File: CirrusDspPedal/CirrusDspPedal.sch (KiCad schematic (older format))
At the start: 0 parts

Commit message: Completed schematic design
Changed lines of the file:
@@
 $Descr A4 11693 8268
 encoding utf-8
-Sheet 1 10
+Sheet 1 11
 Title ""
 Date ""
@@
 F0 "SignalRelay" 50
 F1 "SignalRelay.sch" 50
-F2 "SignalSwitch" I L 5075 1750 50
-F3 "SIGNAL_IN" I L 5075 1300 50
-F4 "SIGNAL_OUT" I R 7050 1300 50
-F5 "FX_IN" I L 5075 1525 50
-F6 "FX_OUT" I R 7050 1525 50
+F2 "SIGNAL_IN" I L 5075 1300 50
+F3 "SIGNAL_OUT" I R 7050 1300 50
+F4 "FX_IN" I L 5075 1525 50
+F5 "FX_OUT" I R 7050 1525 50
+F6 "RelayCoil_OUT" I L 5075 1750 50
 $EndSheet
 Wire Wire Line
@@
 F8 "I2S_LRCK_OUT" I R 7050 3175 50
 F9 "I2S_LRCK_IN" I L 5050 3175 50
-F10 "ExpInput" I L 5050 4325 50
-F11 "SIgnalSwitch" I L 5050 2550 50
-F12 "FootSwitchA" I L 5050 4500 50
-F13 "FootSwitchB" I L 5050 4675 50
-F14 "UserPotA" I L 5050 4850 50
-F15 "UserPotB" I L 5050 5025 50
-F16 "UserSwA" I L 5050 5200 50
-F17 "UserSwB" I L 5050 5375 50
+F10 "UserSwitchB_IN" I L 5050 5375 50
+F11 "UserSwithA_IN" I L 5050 5200 50
+F12 "RelayCoil_OUT" I L 5050 2550 50
+F13 "FootExp_IN" I L 5050 4325 50
+F14 "UserPotA_IN" I L 5050 4850 50
+F15 "UserPotB_IN" I L 5050 5025 50
+F16 "FootSwitchB_IN" I L 5050 4675 50
+F17 "FootSwitchA_IN" I L 5050 4500 50
+F18 "uSD_CMD" I R 7050 4725 50
+F19 "uSD_CLK" I R 7050 4850 50
+F20 "uSD_D0" I R 7050 4275 50
+F21 "uSD_D1" I R 7050 4375 50
+F22 "uSD_D2" I R 7050 4475 50
+F23 "uSD_D3" I R 7050 4575 50
+F24 "uSD_Detect" I R 7050 5050 50
 $EndSheet
 $Sheet
@@
 F0 "ExtInput" 50
 F1 "ExtInput.sch" 50
-F2 "ExpInput" I R 3525 4325 50
-F3 "FootSwitchA" I R 3525 4500 50
-F4 "FootSwitchB" I R 3525 4675 50
-F5 "UserPotA" I R 3525 4850 50
-F6 "UserPotB" I R 3525 5025 50
-F7 "UserSwA" I R 3525 5200 50
-F8 "UserSwB" I R 3525 5375 50
+F2 "FootSwitchA_IN" I R 3525 4500 50
+F3 "FootSwitchB_IN" I R 3525 4675 50
+F4 "UserPotA_IN" I R 3525 4850 50
+F5 "UserPotB_IN" I R 3525 5025 50
+F6 "UserSwitchA_IN" I R 3525 5200 50
+F7 "UserSwitchB_IN" I R 3525 5375 50
+F8 "FootExp_IN" I R 3525 4325 50
 $EndSheet
+$Sheet
+S 8525 4075 1225 1250
+U 5FAF8111
+F0 "MicroSD" 50
+F1 "MicroSD.sch" 50
+F2 "uSD_CLK" I L 8525 4850 50
+F3 "uSD_D0" I L 8525 4275 50
+F4 "uSD_D1" I L 8525 4375 50
+F5 "uSD_D2" I L 8525 4475 50
+F6 "uSD_D3" I L 8525 4575 50
+F7 "uSD_CMD" I L 8525 4725 50
+F8 "uSD_Detect" I L 8525 5050 50
+$EndSheet
+Wire Wire Line
+	8525 4725 7050 4725
+Wire Wire Line
+	8525 4575 7050 4575
+Wire Wire Line
+	8525 4475 7050 4475
+Wire Wire Line
+	8525 4375 7050 4375
+Wire Wire Line
+	8525 4275 7050 4275
+Wire Wire Line
+	8525 4850 7050 4850
+Wire Wire Line
+	8525 5050 7050 5050
 $EndSCHEMATC

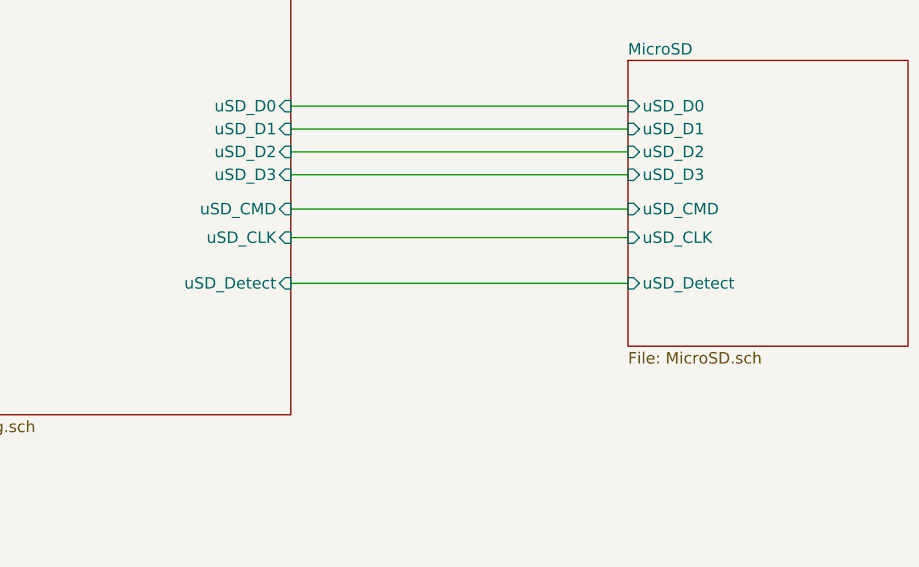
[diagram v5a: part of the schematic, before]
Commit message: replaced SDIO connector
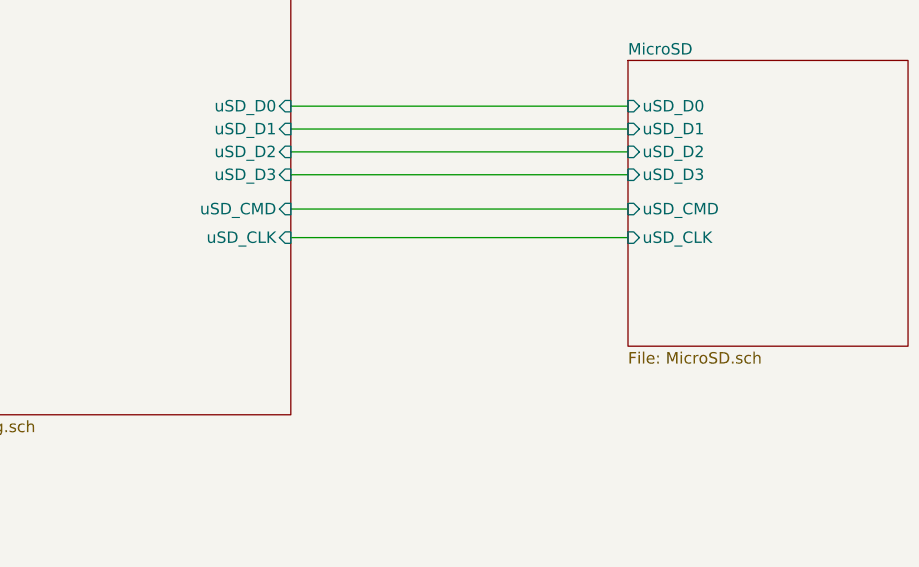
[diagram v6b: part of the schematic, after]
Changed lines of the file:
@@
 F22 "uSD_D2" I R 7050 4475 50
 F23 "uSD_D3" I R 7050 4575 50
-F24 "uSD_Detect" I R 7050 5050 50
 $EndSheet
 $Sheet
@@
 F6 "uSD_D3" I L 8525 4575 50
 F7 "uSD_CMD" I L 8525 4725 50
-F8 "uSD_Detect" I L 8525 5050 50
 $EndSheet
 Wire Wire Line
@@
 Wire Wire Line
 	8525 4850 7050 4850
-Wire Wire Line
-	8525 5050 7050 5050
 $EndSCHEMATC

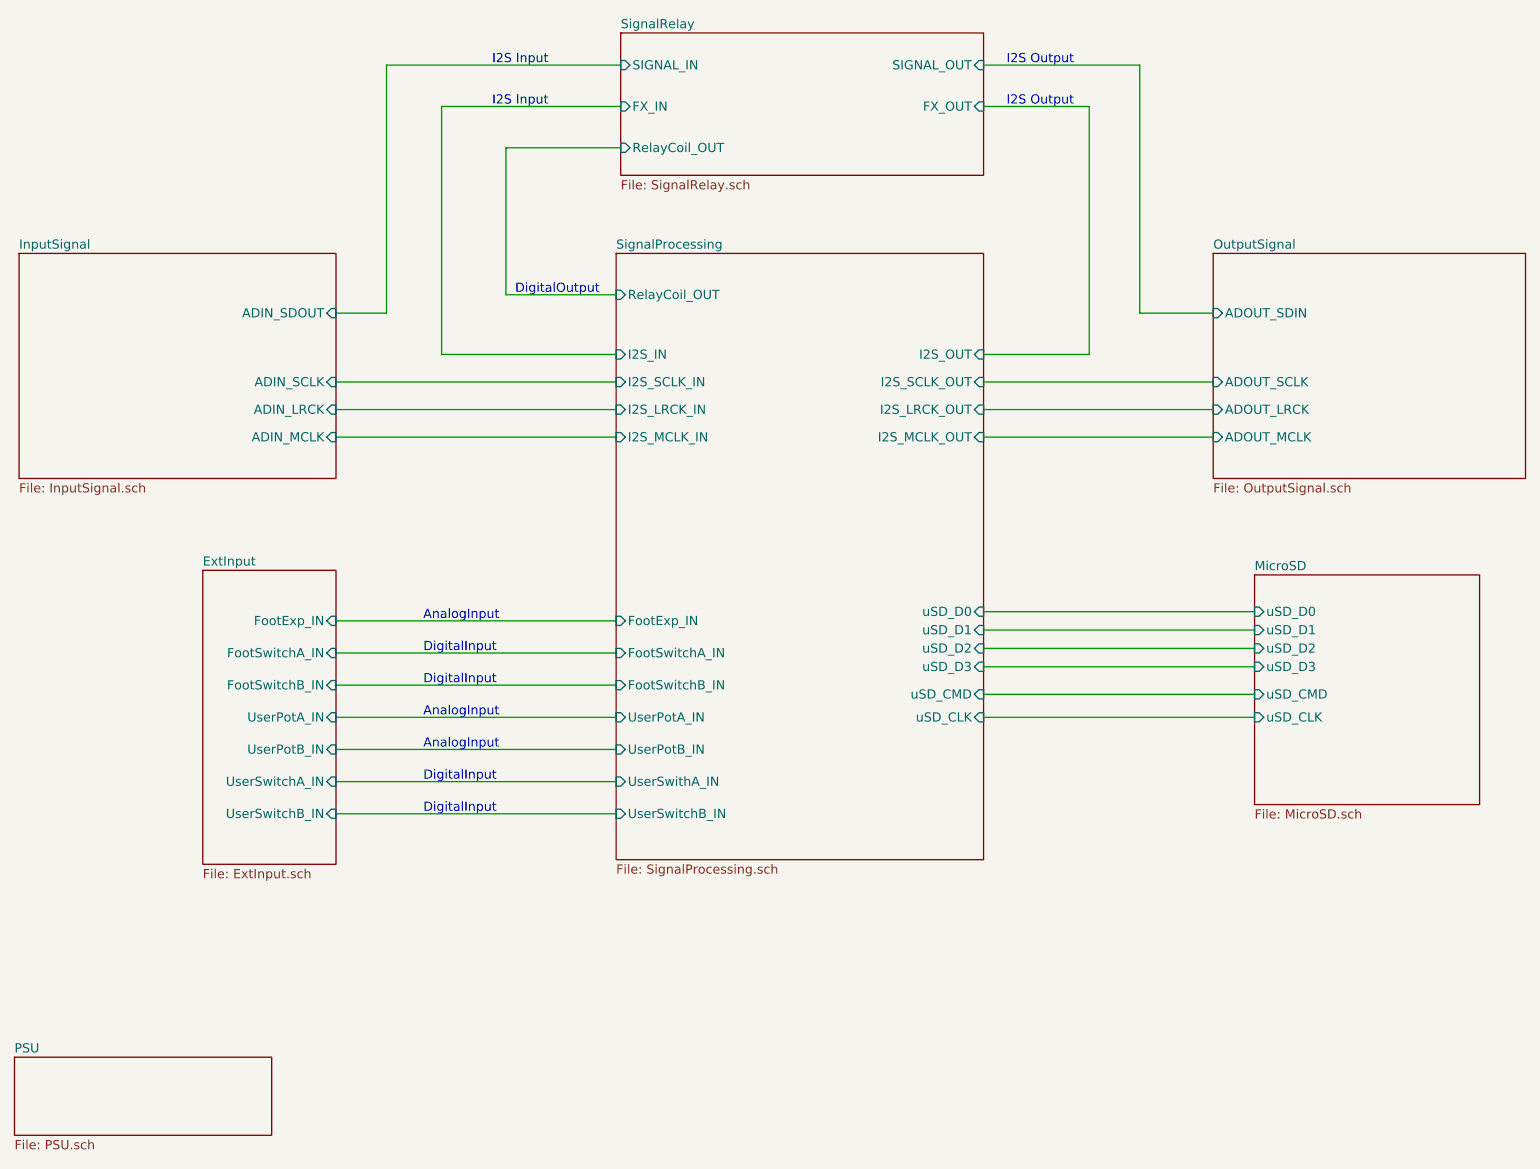
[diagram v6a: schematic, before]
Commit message: Updated RevB
- Replaced analog pots with Rotary Encoders
- Added I2C connector (for OLED screen)
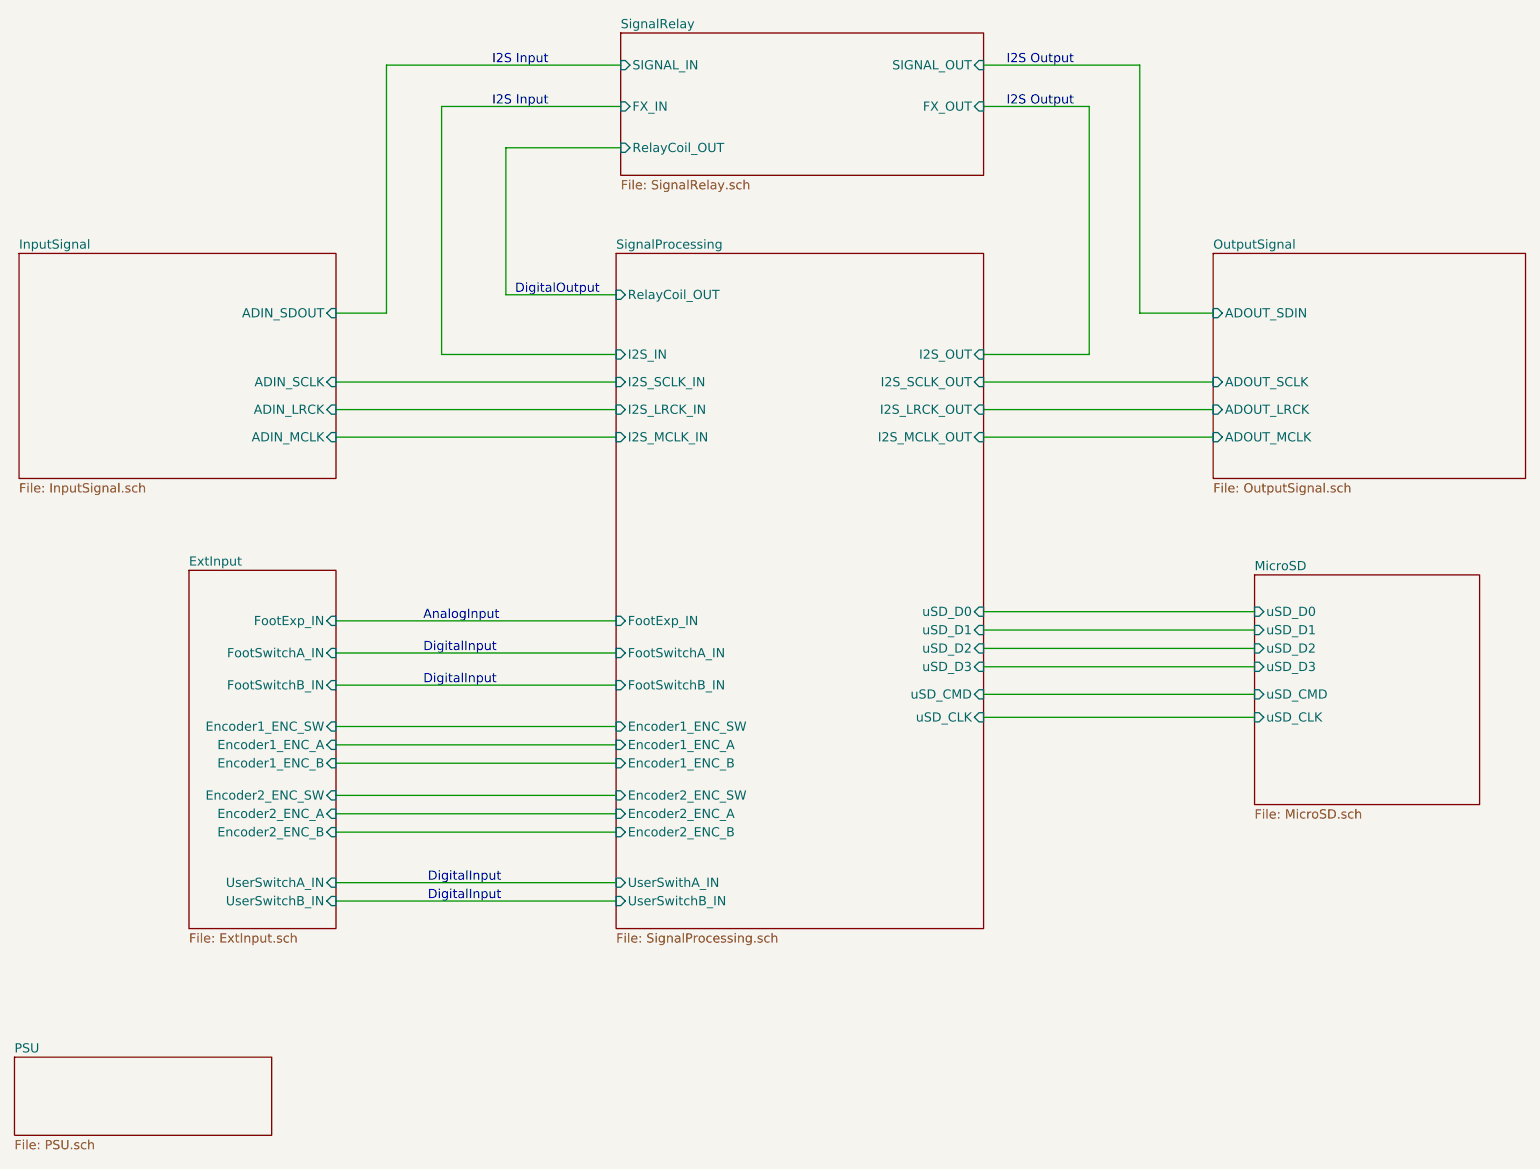
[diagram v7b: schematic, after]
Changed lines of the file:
@@
 $Descr A4 11693 8268
 encoding utf-8
-Sheet 1 10
+Sheet 1 12
 Title ""
 Date ""
@@
 Text Notes 4500 2550 0    50   ~ 0
 DigitalOutput
-Wire Wire Line
-	3525 4850 5050 4850
-Wire Wire Line
-	3525 5025 5050 5025
-Text Notes 4000 4850 0    50   ~ 0
-AnalogInput
-Text Notes 4000 5025 0    50   ~ 0
-AnalogInput
 Text Notes 4375 1300 0    50   ~ 0
 I2S Input
@@
 I2S Output
 Wire Wire Line
-	3525 5200 5050 5200
-Wire Wire Line
-	3525 5375 5050 5375
-Text Notes 4000 5200 0    50   ~ 0
-DigitalInput
-Text Notes 4000 5375 0    50   ~ 0
-DigitalInput
-$Sheet
-S 5050 2325 2000 3300
+	3525 5850 5050 5850
+Text Notes 4025 5750 0    50   ~ 0
+DigitalInput
+Text Notes 4025 5850 0    50   ~ 0
+DigitalInput
+$Sheet
+S 5050 2325 2000 3675
 U 5F834F6D
 F0 "SignalProcessing" 50
@@
 F8 "I2S_LRCK_OUT" I R 7050 3175 50
 F9 "I2S_LRCK_IN" I L 5050 3175 50
-F10 "UserSwitchB_IN" I L 5050 5375 50
-F11 "UserSwithA_IN" I L 5050 5200 50
+F10 "UserSwitchB_IN" I L 5050 5850 50
+F11 "UserSwithA_IN" I L 5050 5750 50
 F12 "RelayCoil_OUT" I L 5050 2550 50
 F13 "FootExp_IN" I L 5050 4325 50
-F14 "UserPotA_IN" I L 5050 4850 50
-F15 "UserPotB_IN" I L 5050 5025 50
-F16 "FootSwitchB_IN" I L 5050 4675 50
-F17 "FootSwitchA_IN" I L 5050 4500 50
-F18 "uSD_CMD" I R 7050 4725 50
-F19 "uSD_CLK" I R 7050 4850 50
-F20 "uSD_D0" I R 7050 4275 50
-F21 "uSD_D1" I R 7050 4375 50
-F22 "uSD_D2" I R 7050 4475 50
-F23 "uSD_D3" I R 7050 4575 50
-$EndSheet
-$Sheet
-S 2800 4050 725  1600
+F14 "FootSwitchB_IN" I L 5050 4675 50
+F15 "FootSwitchA_IN" I L 5050 4500 50
+F16 "uSD_CMD" I R 7050 4725 50
+F17 "uSD_CLK" I R 7050 4850 50
+F18 "uSD_D0" I R 7050 4275 50
+F19 "uSD_D1" I R 7050 4375 50
+F20 "uSD_D2" I R 7050 4475 50
+F21 "uSD_D3" I R 7050 4575 50
+F22 "Encoder1_ENC_A" I L 5050 5000 50
+F23 "Encoder1_ENC_B" I L 5050 5100 50
+F24 "Encoder2_ENC_A" I L 5050 5375 50
+F25 "Encoder2_ENC_B" I L 5050 5475 50
+F26 "Encoder2_ENC_SW" I L 5050 5275 50
+F27 "Encoder1_ENC_SW" I L 5050 4900 50
+$EndSheet
+$Sheet
+S 2725 4050 800  1950
 U 5F898CA5
 F0 "ExtInput" 50
@@
 F2 "FootSwitchA_IN" I R 3525 4500 50
 F3 "FootSwitchB_IN" I R 3525 4675 50
-F4 "UserPotA_IN" I R 3525 4850 50
-F5 "UserPotB_IN" I R 3525 5025 50
-F6 "UserSwitchA_IN" I R 3525 5200 50
-F7 "UserSwitchB_IN" I R 3525 5375 50
-F8 "FootExp_IN" I R 3525 4325 50
+F4 "UserSwitchA_IN" I R 3525 5750 50
+F5 "UserSwitchB_IN" I R 3525 5850 50
+F6 "FootExp_IN" I R 3525 4325 50
+F7 "Encoder1_ENC_SW" I R 3525 4900 50
+F8 "Encoder1_ENC_A" I R 3525 5000 50
+F9 "Encoder1_ENC_B" I R 3525 5100 50
+F10 "Encoder2_ENC_SW" I R 3525 5275 50
+F11 "Encoder2_ENC_A" I R 3525 5375 50
+F12 "Encoder2_ENC_B" I R 3525 5475 50
 $EndSheet
 $Sheet
@@
 Wire Wire Line
 	8525 4850 7050 4850
+Wire Wire Line
+	3525 5750 5050 5750
+Wire Wire Line
+	3525 5000 5050 5000
+Wire Wire Line
+	3525 5100 5050 5100
+Wire Wire Line
+	3525 5375 5050 5375
+Wire Wire Line
+	3525 5475 5050 5475
+Wire Wire Line
+	3525 5275 5050 5275
+Wire Wire Line
+	5050 4900 3525 4900
 $EndSCHEMATC
